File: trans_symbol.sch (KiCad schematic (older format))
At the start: 17 parts, among them J1 Conn_01x19, J2 Conn_01x19, J3 USB_B_Micro, U1 ATSAMD21G18A-AU, U2 MIC5504-3.3YM5, Y1 32768Hz

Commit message: start working on spokes
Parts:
- removed J1, J2: Conn_01x19, Connector_PinHeader_2.54mm:PinHeader_1x19_P2.54mm_Vertical, symbol Connector_Generic:Conn_01x19
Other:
- note removed: "Breakout pins"
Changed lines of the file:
@@
 Text GLabel 3950 1350 0    50   Input ~ 0
-RESET
-Text GLabel 8850 2450 0    50   Input ~ 0
-PA23
-Text GLabel 8850 2750 0    50   Input ~ 0
-PA27
-Text GLabel 8850 2950 0    50   Input ~ 0
-PA28
-Text GLabel 8150 1450 2    50   Input ~ 0
-PA30
-Text GLabel 8150 1550 2    50   Input ~ 0
-PA31
-Text GLabel 8850 2650 0    50   Input ~ 0
-PB23
-Text GLabel 8850 2550 0    50   Input ~ 0
-PB22
-Text GLabel 8850 1250 0    50   Input ~ 0
-PB11
-Text GLabel 8850 1150 0    50   Input ~ 0
-PB10
-Text GLabel 8150 2150 2    50   Input ~ 0
-PB09
-Text GLabel 8150 2050 2    50   Input ~ 0
-PB08
-Text GLabel 8150 1750 2    50   Input ~ 0
-PB03
-Text GLabel 8150 1650 2    50   Input ~ 0
-PB02
-$Comp
-L power:VBUS #PWR0117
-U 1 1 5EC319EB
-P 8150 1150
-F 0 "#PWR0117" H 8150 1000 50  0001 C CNN
-F 1 "VBUS" V 8165 1278 50  0000 L CNN
-F 2 "" H 8150 1150 50  0001 C CNN
-F 3 "" H 8150 1150 50  0001 C CNN
-	1    8150 1150
-	0    1    1    0
-$EndComp
-$Comp
-L power:+3.3V #PWR0118
-U 1 1 5EC31EF3
-P 8150 1250
-F 0 "#PWR0118" H 8150 1100 50  0001 C CNN
-F 1 "+3.3V" V 8165 1378 50  0000 L CNN
-F 2 "" H 8150 1250 50  0001 C CNN
-F 3 "" H 8150 1250 50  0001 C CNN
-	1    8150 1250
-	0    1    1    0
-$EndComp
-$Comp
-L power:GND #PWR0119
-U 1 1 5EC32415
-P 8150 1350
-F 0 "#PWR0119" H 8150 1100 50  0001 C CNN
-F 1 "GND" V 8155 1222 50  0000 R CNN
-F 2 "" H 8150 1350 50  0001 C CNN
-F 3 "" H 8150 1350 50  0001 C CNN
-	1    8150 1350
-	0    -1   -1   0
-$EndComp
-Text GLabel 8850 2850 0    50   Input ~ 0
 RESET
 Wire Wire Line
@@
 Text GLabel 3950 1850 0    50   Input ~ 0
 PA02
-Text GLabel 8150 1850 2    50   Input ~ 0
-PA02
-Text GLabel 8850 2350 0    50   Input ~ 0
-PA22
-Text GLabel 8850 2250 0    50   Input ~ 0
-PA21
-Text GLabel 8850 2150 0    50   Input ~ 0
-PA20
-Text GLabel 8850 2050 0    50   Input ~ 0
-PA19
-Text GLabel 8850 1950 0    50   Input ~ 0
-PA18
-Text GLabel 8850 1850 0    50   Input ~ 0
-PA17
-Text GLabel 8850 1750 0    50   Input ~ 0
-PA16
-Text GLabel 8850 1650 0    50   Input ~ 0
-PA15
-Text GLabel 8850 1550 0    50   Input ~ 0
-PA14
-Text GLabel 8850 1450 0    50   Input ~ 0
-PA13
-Text GLabel 8850 1350 0    50   Input ~ 0
-PA12
-Text GLabel 8150 2950 2    50   Input ~ 0
-PA11
-Text GLabel 8150 2850 2    50   Input ~ 0
-PA10
-Text GLabel 8150 2750 2    50   Input ~ 0
-PA09
-Text GLabel 8150 2650 2    50   Input ~ 0
-PA08
-Text GLabel 8150 2550 2    50   Input ~ 0
-PA07
-Text GLabel 8150 2450 2    50   Input ~ 0
-PA06
-Text GLabel 8150 2350 2    50   Input ~ 0
-PA05
-Text GLabel 8150 2250 2    50   Input ~ 0
-PA04
-Text GLabel 8150 1950 2    50   Input ~ 0
-PA03
 Wire Notes Line
 	850  -200 850  4750
 Wire Notes Line
 	2800 -200 2800 4750
-Text Notes 7550 800  0    50   ~ 0
-Breakout pins
 Wire Notes Line
 	7200 -200 7200 4750
@@
 Text GLabel 3950 4150 0    50   Input ~ 0
 USB_D+
-$Comp
-L Connector_Generic:Conn_01x19 J2
-U 1 1 5EC6EBC8
-P 9050 2050
-F 0 "J2" H 9000 3200 50  0000 L CNN
-F 1 "Conn_01x19" H 8800 3100 50  0000 L CNN
-F 2 "Connector_PinHeader_2.54mm:PinHeader_1x19_P2.54mm_Vertical" H 9050 2050 50  0001 C CNN
-F 3 "~" H 9050 2050 50  0001 C CNN
-	1    9050 2050
-	1    0    0    -1
-$EndComp
-$Comp
-L Connector_Generic:Conn_01x19 J1
-U 1 1 5EC7617E
-P 7950 2050
-F 0 "J1" H 7900 3200 50  0000 L CNN
-F 1 "Conn_01x19" H 7700 3100 50  0000 L CNN
-F 2 "Connector_PinHeader_2.54mm:PinHeader_1x19_P2.54mm_Vertical" H 7950 2050 50  0001 C CNN
-F 3 "~" H 7950 2050 50  0001 C CNN
-	1    7950 2050
-	-1   0    0    -1
-$EndComp
 Connection ~ 5500 1950
 $Comp

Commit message: fix pixel orientation on arrow; add via for GND out of each LED (we cannot delete vias programmatically due to a crasher, so layout is manual from here on out); choose pins for SPI; wire up SPI & USB data
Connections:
- net labels added: PA17_MISO, PA19_SCK, PA20_MOSI
- net labels removed: PA17, PA19, PA20
- wire segments 46 -> 48
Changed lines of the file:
@@
 EESchema Schematic File Version 4
-EELAYER 29 0
+EELAYER 30 0
 EELAYER END
 $Descr A4 11693 8268
@@
 PA16
 Text GLabel 3950 3350 0    50   Input ~ 0
-PA17
+PA17_MISO
 Text GLabel 3950 3450 0    50   Input ~ 0
 PA18
 Text GLabel 3950 3550 0    50   Input ~ 0
-PA19
+PA19_SCK
 Text GLabel 3950 3650 0    50   Input ~ 0
-PA20
+PA20_MOSI
 Text GLabel 3950 3750 0    50   Input ~ 0
 PA21
@@
 Connection ~ 5350 1550
 $Sheet
-S 1000 6200 1400 750
+S 1350 5050 1400 750
 U 5F81AC32
 F0 "Sheet5F81AC31" 50
 F1 "leds.sch" 50
+F2 "LED_SCK" I L 1350 5200 50
+F3 "LED_DATA" I L 1350 5300 50
 $EndSheet
+Text GLabel 1250 5300 0    50   Input ~ 0
+PA20_MOSI
+Text GLabel 1250 5200 0    50   Input ~ 0
+PA19_SCK
+Wire Wire Line
+	1350 5200 1250 5200
+Wire Wire Line
+	1250 5300 1350 5300
 $EndSCHEMATC

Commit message: first pass on manual layout of board including led power traces & samd circuitry; key idea: take out the usb port and solder the usb data & power directly to the board, i.e. it'll have its own cable attached, possibly a short cable with the usb plug on it so that I can use various length usb cables
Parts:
- removed J3: USB_B_Micro, Connector_USB:USB_Micro-B_Molex-105017-0001, symbol Connector:USB_B_Micro
- added J4: Conn_01x04, Connector_PinHeader_1.27mm:PinHeader_1x04_P1.27mm_Vertical, symbol Connector_Generic:Conn_01x04
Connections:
- net labels added: VDDANA, VDDCORE
- net labels removed: PA02, PA03, PA04, PA05, PA06, PA07, PA08, PA09, PA10, PA11, PA12, PA13, PA14, PA15, PA16, PA18, PA19_SCK, PA20_MOSI, PA21, PA22, PA23, PA27, PA28, PA30, PA31, PB02, PB03, PB08, PB09, PB10, PB11, PB22, PB23
- wire segments 48 -> 54
- no-connect marks 2 -> 32
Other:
- note added: "USB Power Regulator"
- note removed: "USB & USB Power Regulator"
- moved on the sheet: C5

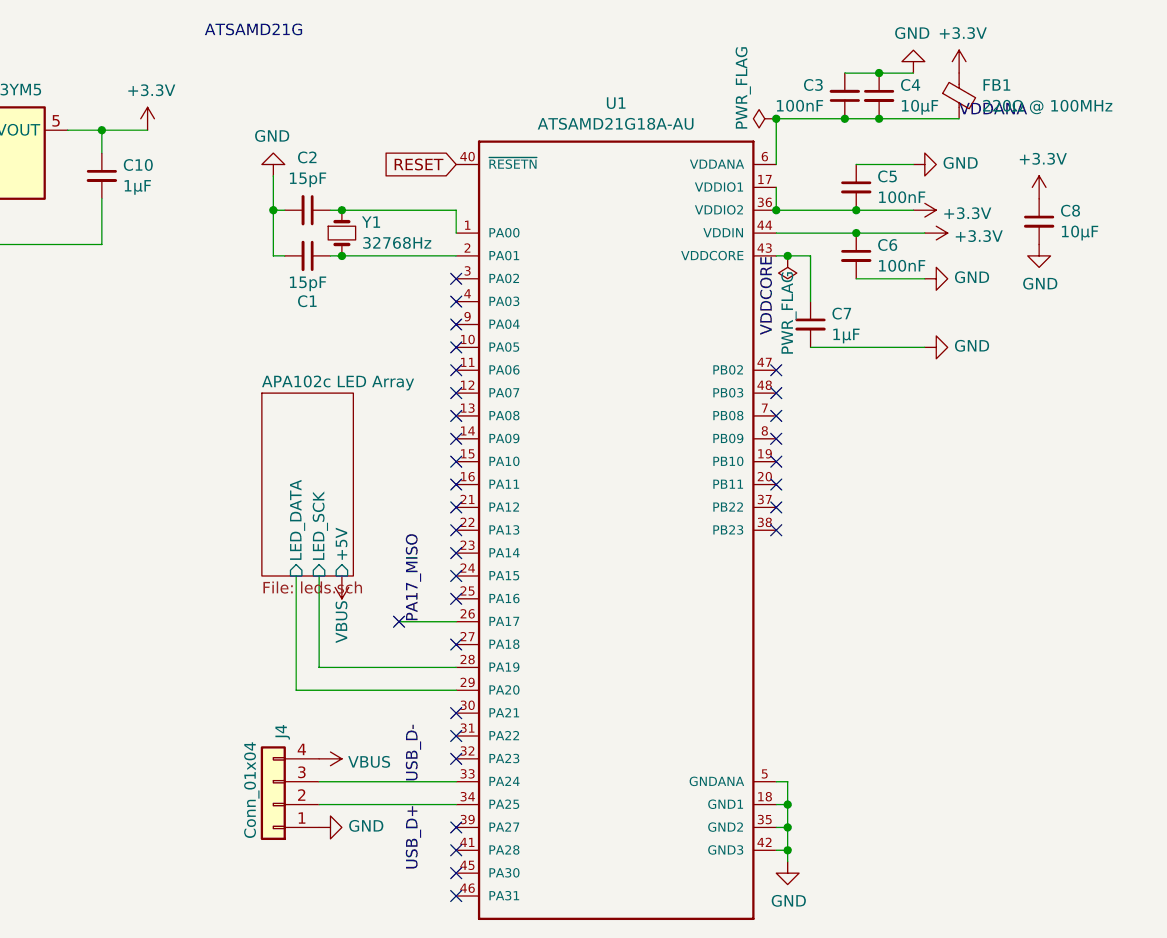
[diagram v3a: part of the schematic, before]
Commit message: add a decoupling capacitor on +5V for LEDs
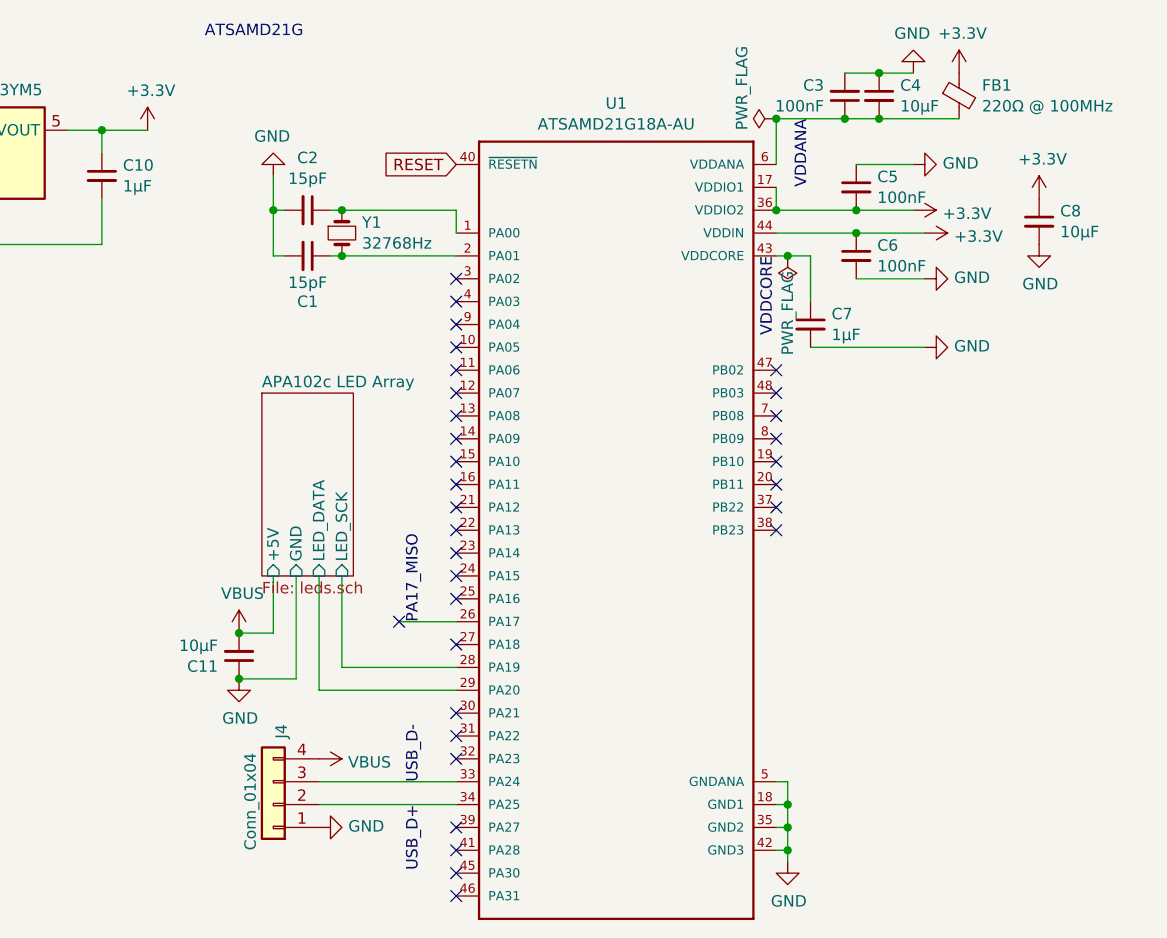
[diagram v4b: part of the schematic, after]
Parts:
- added C11: 10µF, Capacitor_SMD:C_0402_1005Metric, symbol Device:C_Small
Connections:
- net GND: now also C11.1
- net VBUS: now also C11.2
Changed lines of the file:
@@
 Wire Wire Line
 	5350 1450 5350 1550
-$Sheet
-S 3100 2350 400  800
-U 5F81AC32
-F0 "APA102c LED Array" 50
-F1 "leds.sch" 50
-F2 "LED_SCK" I B 3350 3150 50
-F3 "LED_DATA" I B 3250 3150 50
-F5 "+5V" I B 3450 3150 50
-$EndSheet
 $Comp
 L power:VBUS #PWR0103
@@
 	0    1    1    0
 $EndComp
-Text Label 6150 1150 0    50   ~ 0
+Text Label 5500 1150 3    50   ~ 0
 VDDANA
 Wire Wire Line
@@
 	5400 1750 5500 1750
 $Comp
-L power:VBUS #PWR?
-U 1 1 5FA777BA
-P 3450 3150
-F 0 "#PWR?" H 3450 3000 50  0001 C CNN
-F 1 "VBUS" V 3450 3350 50  0000 C CNN
-F 2 "" H 3450 3150 50  0001 C CNN
-F 3 "" H 3450 3150 50  0001 C CNN
-	1    3450 3150
-	-1   0    0    1
-$EndComp
-$Comp
 L Connector_Generic:Conn_01x04 J4
 U 1 1 5F9E60C8
 P 3150 4150
 F 0 "J4" V 3114 3862 50  0000 R CNN
-F 1 "Conn_01x04" V 3250 4300 50  0000 R CNN
+F 1 "Conn_01x04" V 3250 4350 50  0000 R CNN
 F 2 "Connector_PinHeader_1.27mm:PinHeader_1x04_P1.27mm_Vertical" H 3150 4150 50  0001 C CNN
 F 3 "~" H 3150 4150 50  0001 C CNN
@@
 PA17_MISO
 Wire Wire Line
-	3350 3150 3350 3550
+	3450 3150 3450 3550
 Wire Wire Line
-	3250 3650 3250 3150
+	3350 3650 3350 3150
+$Comp
+L Device:C_Small C11
+U 1 1 5FBCCF61
+P 3000 3500
+F 0 "C11" H 2908 3546 50  0000 R CNN
+F 1 "10µF" H 2908 3455 50  0000 R CNN
+F 2 "Capacitor_SMD:C_0402_1005Metric" H 3000 3500 50  0001 C CNN
+F 3 "~" H 3000 3500 50  0001 C CNN
+	1    3000 3500
+	1    0    0    1
+$EndComp
 Wire Wire Line
-	3250 3650 3950 3650
+	3350 3650 3950 3650
 Wire Wire Line
-	3350 3550 3950 3550
+	3450 3550 3950 3550
+$Sheet
+S 3100 2350 400  800
+U 5F81AC32
+F0 "APA102c LED Array" 50
+F1 "leds.sch" 50
+F2 "LED_SCK" I B 3450 3150 50
+F3 "LED_DATA" I B 3350 3150 50
+F4 "+5V" I B 3150 3150 50
+F5 "GND" I B 3250 3150 50
+$EndSheet
+Wire Wire Line
+	3250 3600 3000 3600
+Wire Wire Line
+	3000 3400 3150 3400
+$Comp
+L power:VBUS #PWR0124
+U 1 1 5FBE76C1
+P 3000 3400
+F 0 "#PWR0124" H 3000 3250 50  0001 C CNN
+F 1 "VBUS" H 3015 3573 50  0000 C CNN
+F 2 "" H 3000 3400 50  0001 C CNN
+F 3 "" H 3000 3400 50  0001 C CNN
+	1    3000 3400
+	1    0    0    -1
+$EndComp
+Connection ~ 3000 3400
+$Comp
+L power:GND #PWR0127
+U 1 1 5FBE7E85
+P 3000 3600
+F 0 "#PWR0127" H 3000 3350 50  0001 C CNN
+F 1 "GND" H 3005 3427 50  0000 C CNN
+F 2 "" H 3000 3600 50  0001 C CNN
+F 3 "" H 3000 3600 50  0001 C CNN
+	1    3000 3600
+	1    0    0    -1
+$EndComp
+Connection ~ 3000 3600
+Wire Wire Line
+	3250 3150 3250 3600
+Wire Wire Line
+	3150 3400 3150 3150
 $EndSCHEMATC

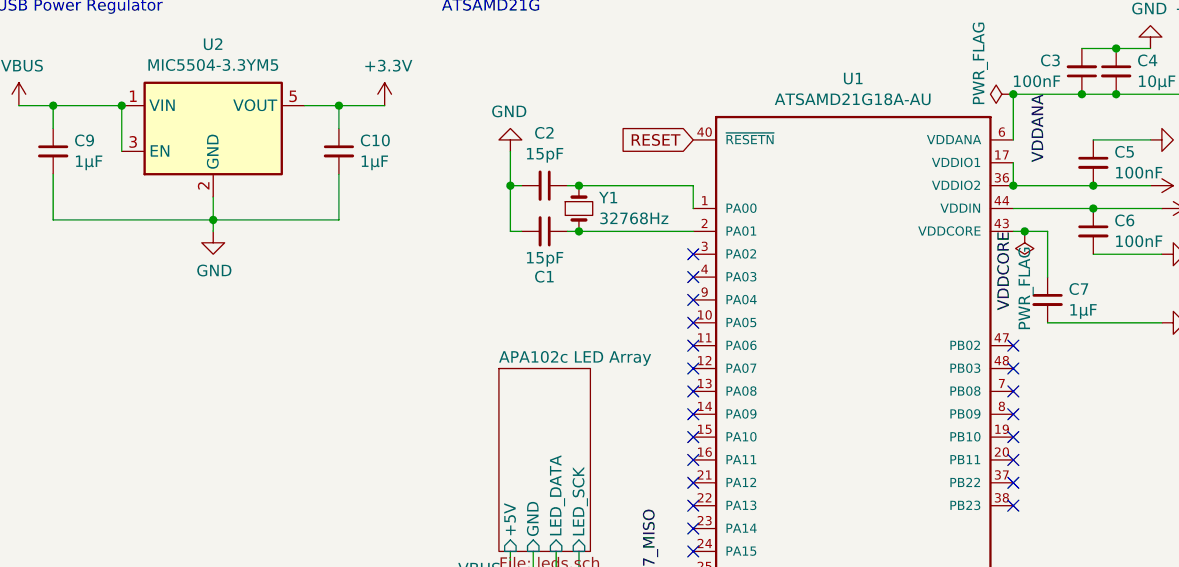
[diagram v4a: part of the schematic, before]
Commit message: re-layout chip circuitry to clean it up a bit and make room for a button on each spoke; add a stub for a button
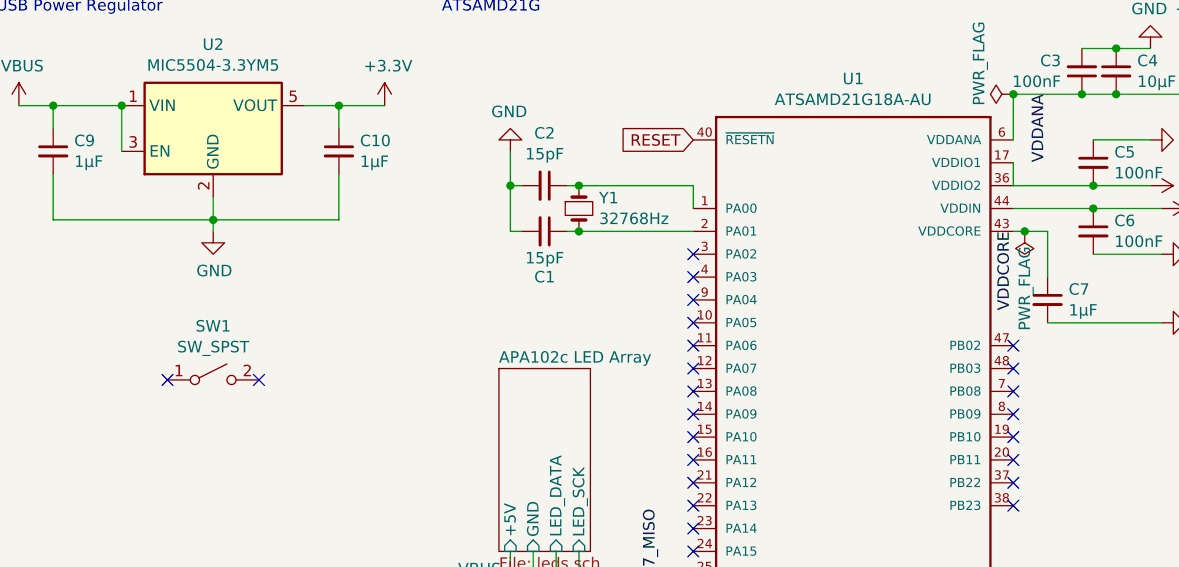
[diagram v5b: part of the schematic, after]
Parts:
- added SW1: SW_SPST, Button_Switch_THT:SW_PUSH_6mm_H5mm, symbol Switch:SW_SPST
- U1: footprint ATSAMD21G18A-AU:QFP50P900X900X120-48N -> ATSAMD21G18A-AU:ATSAMD21G18A-AU
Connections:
- no-connect marks 32 -> 34
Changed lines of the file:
@@
 NoConn ~ 3950 4450
 NoConn ~ 3950 4550
-Connection ~ 5350 1550
-$Comp
-L ATSAMD21G18A-AU:ATSAMD21G18A-AU U1
-U 1 1 5EB21719
-P 4650 2950
-F 0 "U1" H 4650 4817 50  0000 C CNN
-F 1 "ATSAMD21G18A-AU" H 4650 4726 50  0000 C CNN
-F 2 "ATSAMD21G18A-AU:QFP50P900X900X120-48N" H 4650 2950 50  0001 L BNN
-F 3 "ATMEL" H 4650 2950 50  0001 L BNN
-	1    4650 2950
-	1    0    0    -1
-$EndComp
 Wire Wire Line
 	3950 3350 3700 3350
@@
 Wire Wire Line
 	3150 3400 3150 3150
+$Comp
+L Switch:SW_SPST SW1
+U 1 1 5FC0D3F5
+P 1850 2400
+F 0 "SW1" H 1850 2635 50  0000 C CNN
+F 1 "SW_SPST" H 1850 2544 50  0000 C CNN
+F 2 "Button_Switch_THT:SW_PUSH_6mm_H5mm" H 1850 2400 50  0001 C CNN
+F 3 "~" H 1850 2400 50  0001 C CNN
+	1    1850 2400
+	1    0    0    -1
+$EndComp
+NoConn ~ 2050 2400
+NoConn ~ 1650 2400
+$Comp
+L ATSAMD21G18A-AU:ATSAMD21G18A-AU U1
+U 1 1 5EB21719
+P 4650 2950
+F 0 "U1" H 4650 4817 50  0000 C CNN
+F 1 "ATSAMD21G18A-AU" H 4650 4726 50  0000 C CNN
+F 2 "ATSAMD21G18A-AU:ATSAMD21G18A-AU" H 4650 2950 50  0001 L BNN
+F 3 "ATMEL" H 4650 2950 50  0001 L BNN
+	1    4650 2950
+	1    0    0    -1
+$EndComp
 $EndSCHEMATC
